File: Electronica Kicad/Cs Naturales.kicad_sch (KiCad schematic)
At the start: 13 parts, among them M1 Motor_DC

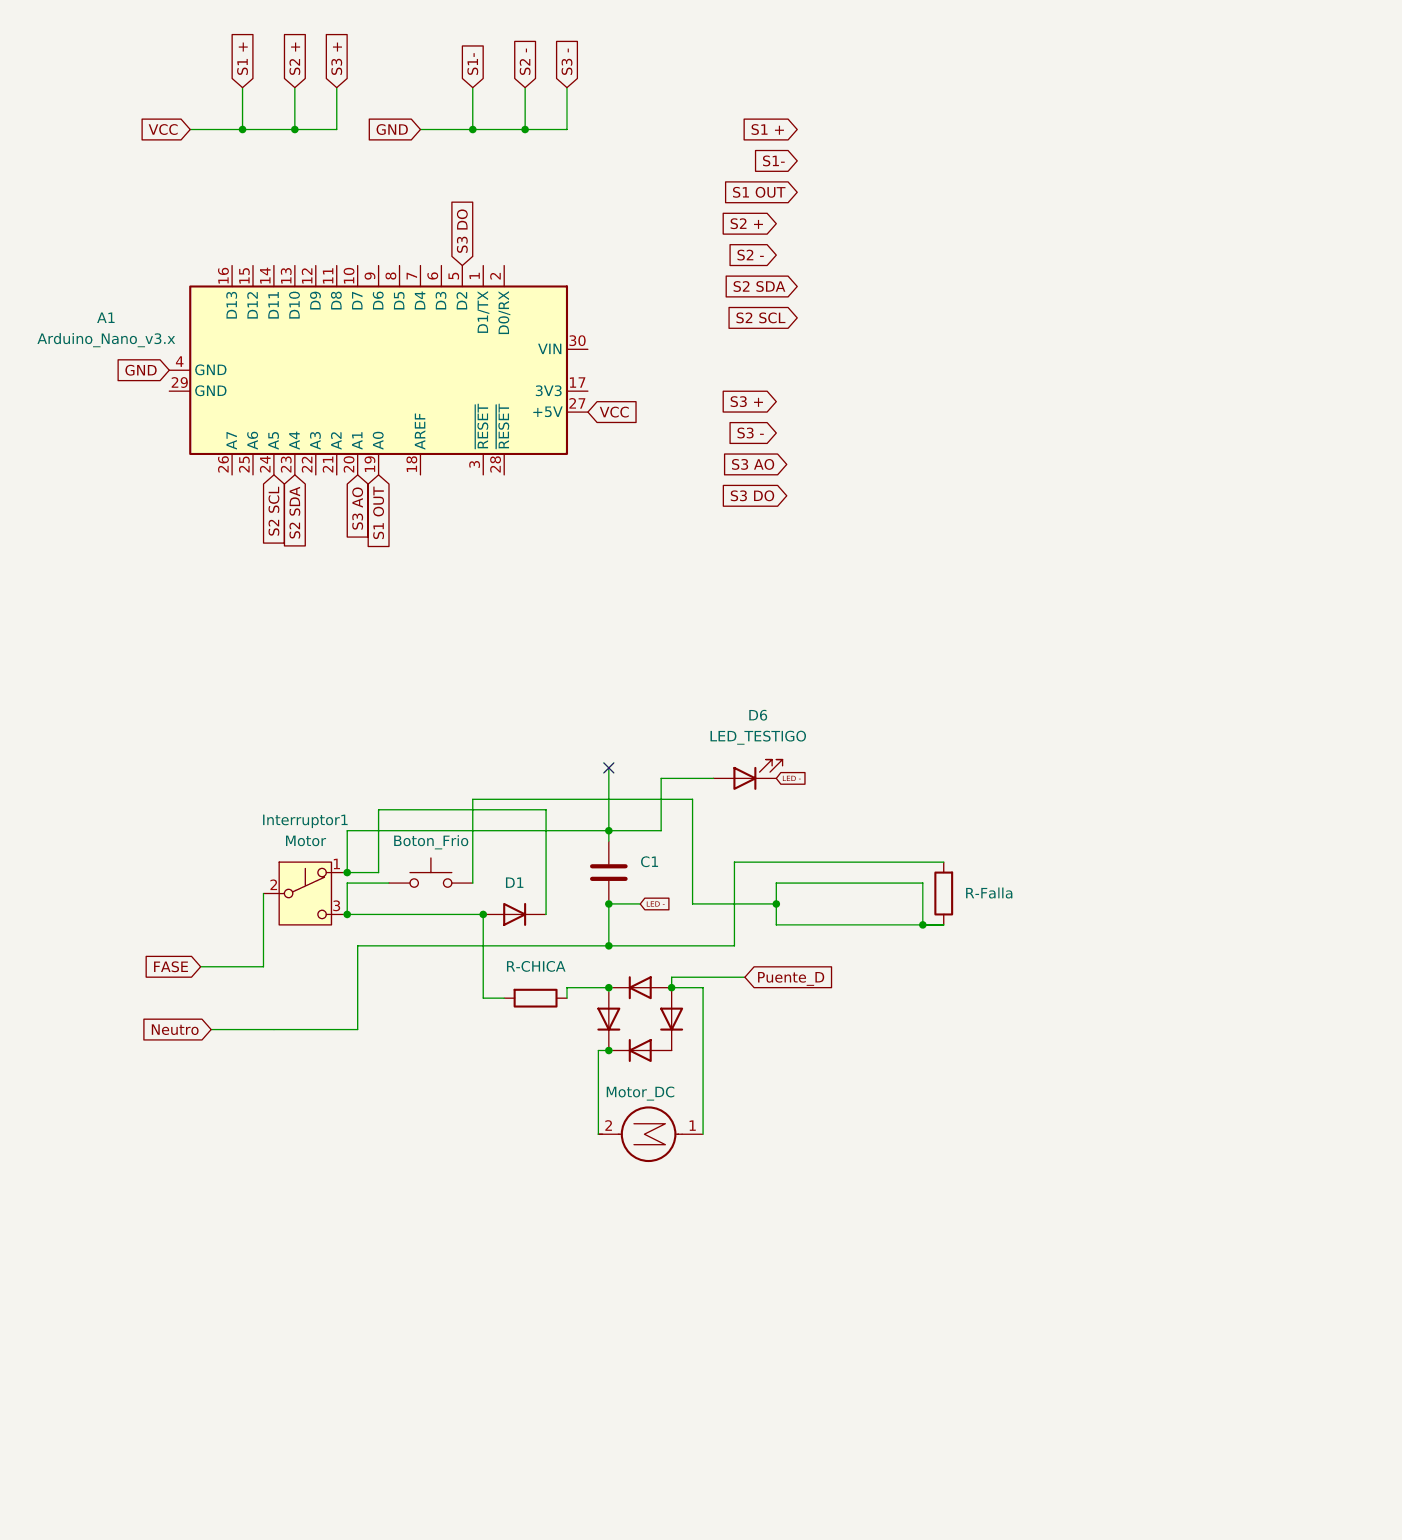
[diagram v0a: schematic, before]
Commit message: Modifico Archivo Esquematico y agrego ESP32 MOD
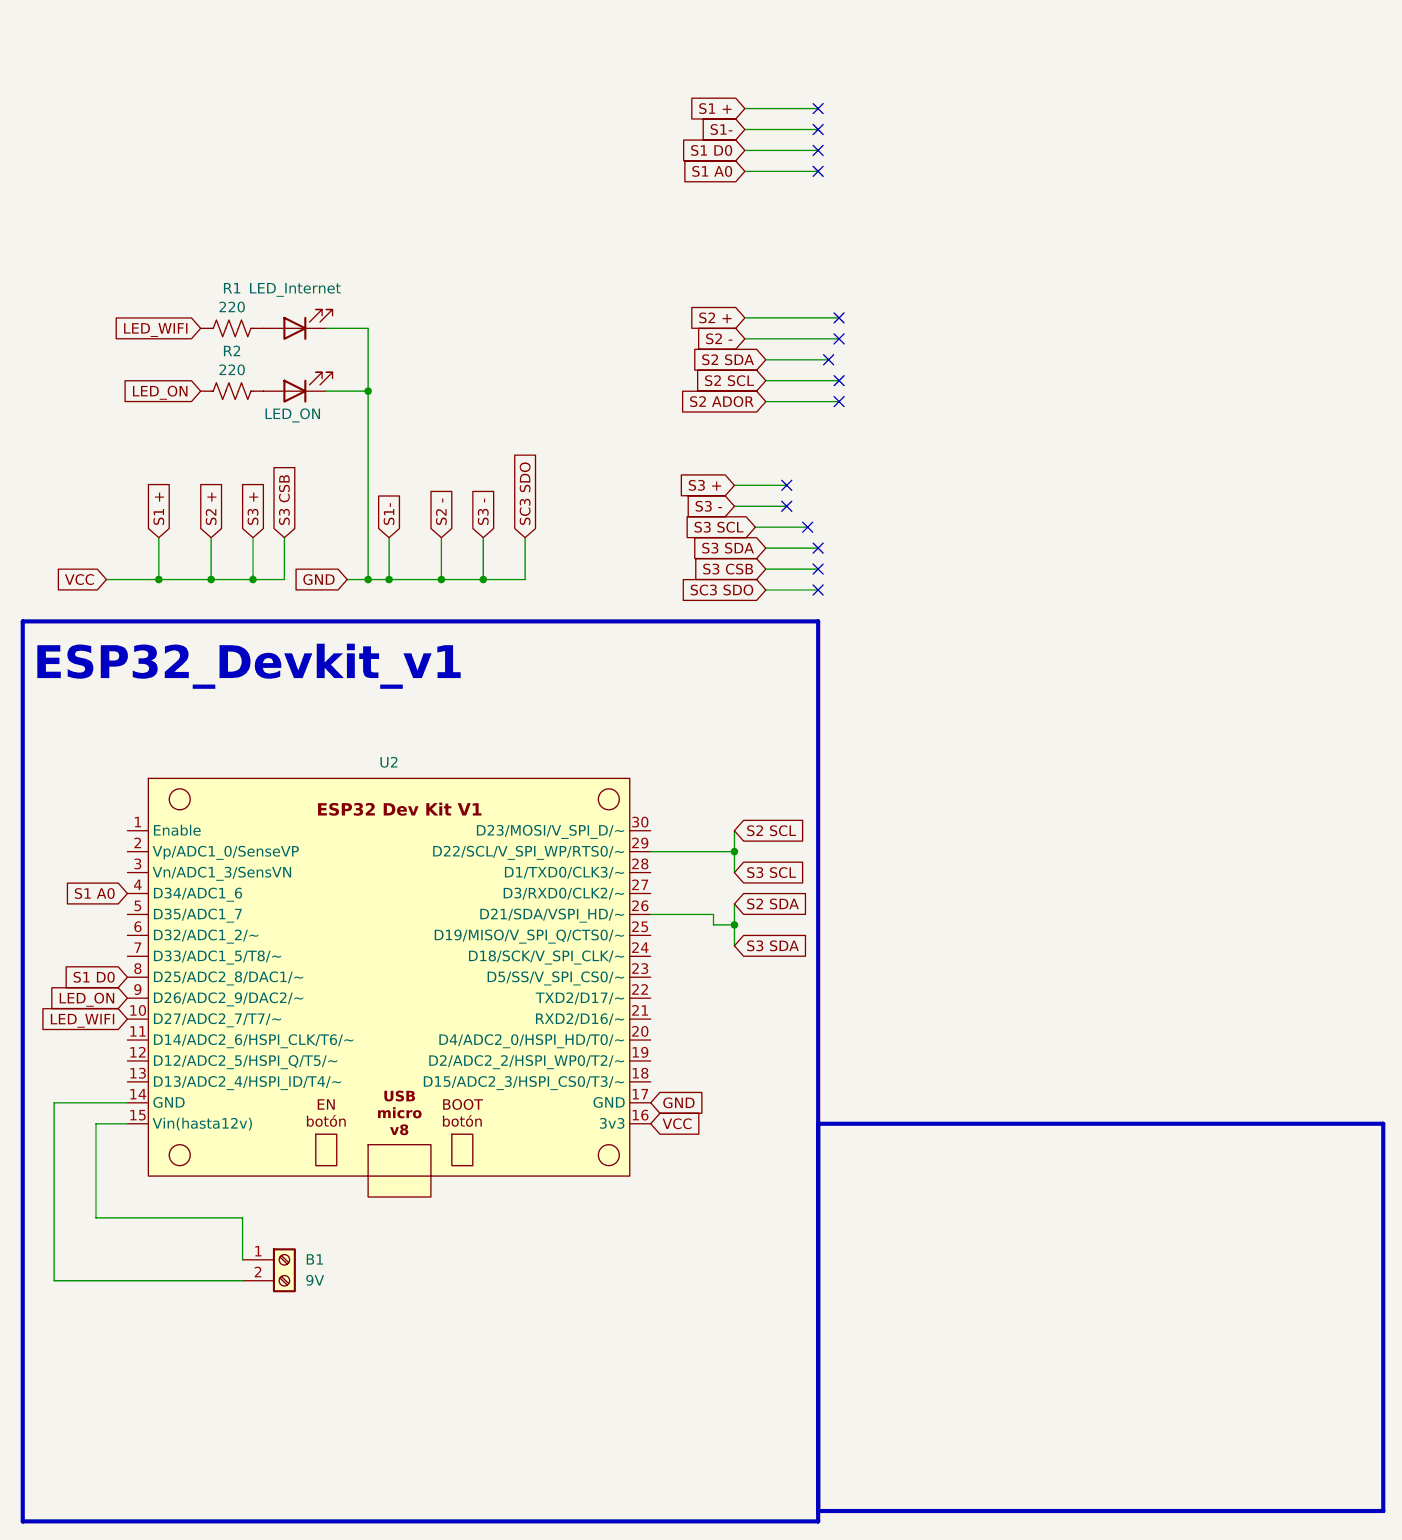
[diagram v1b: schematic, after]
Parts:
- removed A1: Arduino_Nano_v3.x, Module:Arduino_Nano, symbol MCU_Module:Arduino_Nano_v3.x
- removed Boton_Frio: SW_Push, symbol Switch:SW_Push
- removed C1: C, symbol Device:C
- removed D1, D3, D4, D5: D, symbol Device:D
- removed D2: D1, symbol Device:D
- removed D6: LED_TESTIGO, symbol Device:LED
- removed Interruptor1: Motor, symbol Switch:SW_Push_SPDT
- removed M1: Motor_DC, symbol Motor:Motor_DC
- removed R1: R-CHICA, symbol Device:R
- removed R3: R-Falla, symbol Device:R
- added B1: 9V, symbol Connector:Screw_Terminal_01x02
- added D1: LED_ON, symbol Device:LED
- added D2: LED_Internet, symbol Device:LED
- added R1, R2: 220, symbol Device:R_US
- added U2: ~, Librerias:ESP32-DevKit_V1, symbol EME:ESP32_DevKit_V1
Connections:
- net GND: now also D1.1 (K), D2.1 (K), U2.17 (GND)
- net S1 +: now also U2.16 (3v3)
- net S2 SCL: now also U2.29 (D22/SCL/V_SPI_WP/RTS0/~)
- net S2 SDA: now also U2.26 (D21/SDA/VSPI_HD/~)
- new net: D1.2 (A), R2.2
- new net: D2.2 (A), R1.2
- new net: B1.2 (Pin_2), U2.14 (GND)
- new net: B1.1 (Pin_1), U2.15 (Vin(hasta12v))
- new net LED_ON: R2.1, U2.9 (D26/ADC2_9/DAC2/~)
- new net LED_WIFI: R1.1, U2.10 (D27/ADC2_7/T7/~)
- new net S1 A0: U2.4 (D34/ADC1_6)
- new net S1 D0: U2.8 (D25/ADC2_8/DAC1/~)
- no-connect marks 1 -> 15
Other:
- note added: "ESP32_Devkit_v1"

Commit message: Modifico archivo Kicad
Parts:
- added D3: D, Diode_THT:D_DO-41_SOD81_P10.16mm_Horizontal, symbol Device:D
- B1: footprint (none) -> TerminalBlock_Phoenix:TerminalBlock_Phoenix_MKDS-1,5-2-5.08_1x02_P5.08mm_Horizontal
- D1: footprint (none) -> LED_THT:LED_D5.0mm
- D2: footprint (none) -> LED_THT:LED_D5.0mm_Clear
- M1: renamed from U2; footprint Librerias:ESP32-DevKit_V1 -> Librerias1:ESP32-DevKit_V1
- R1, R2: footprint (none) -> Resistor_THT:R_Axial_DIN0204_L3.6mm_D1.6mm_P5.08mm_Horizontal
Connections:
- net at M1.15 (Vin(hasta12v)): now also D3.1 (K); no longer B1.1 (Pin_1)
- new net: B1.1 (Pin_1), D3.2 (A)
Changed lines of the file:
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@@
+	(wire
+		(pts
+			(xy 35.56 161.29) (xy 39.37 161.29)
+		)
+		(stroke
+			(width 0)
+			(type default)
+			(color 255 0 0 1)
+		)
+	)
 	(wire
 		(pts
@@
 	(wire
 		(pts
+			(xy 21.59 161.29) (xy 27.94 161.29)
+		)
+		(stroke
+			(width 0)
+			(type default)
+			(color 255 0 0 1)
+		)
+	)
+	(wire
+		(pts
 			(xy 54.61 60.96) (xy 54.61 83.82)
 		)
@@
 			(width 0)
 			(type default)
-		)
-	)
-	(wire
-		(pts
-			(xy 21.59 161.29) (xy 39.37 161.29)
-		)
-		(stroke
-			(width 0)
-			(type default)
-			(color 255 0 0 1)
 		)
 	)
@@
 			)
 		)
-		(property "Footprint" ""
+		(property "Footprint" "LED_THT:LED_D5.0mm"
 			(at 45.72 60.96 0)
 			(effects
@@
 			)
 		)
-		(property "Footprint" ""
+		(property "Footprint" "Resistor_THT:R_Axial_DIN0204_L3.6mm_D1.6mm_P5.08mm_Horizontal"
 			(at 38.354 52.324 90)
 			(effects
@@
 		(dnp no)
 		(fields_autoplaced yes)
-		(property "Reference" "U2"
-			(at 57.15 106.045 0)
+		(property "Reference" "M1"
+			(at 57.15 105.41 0)
 			(effects
 				(font
@@
 					(size 1.27 1.27)
 				)
-			)
-		)
-		(property "Footprint" "Librerias:ESP32-DevKit_V1"
+				(hide yes)
+			)
+		)
+		(property "Footprint" "Librerias1:ESP32-DevKit_V1"
 			(at 58.42 105.41 0)
 			(effects
@@
 			(project "Cs Naturales"
 				(path "/11f292c7-2d24-408b-b314-b6582b54f0a5"
-					(reference "U2")
+					(reference "M1")
 					(unit 1)
 				)
@@
 			)
 		)
-		(property "Footprint" ""
+		(property "Footprint" "LED_THT:LED_D5.0mm_Clear"
 			(at 45.72 53.34 0)
 			(effects
@@
 			)
 		)
-		(property "Footprint" ""
+		(property "Footprint" "TerminalBlock_Phoenix:TerminalBlock_Phoenix_MKDS-1,5-2-5.08_1x02_P5.08mm_Horizontal"
 			(at 44.45 166.37 0)
 			(effects
@@
 				(path "/11f292c7-2d24-408b-b314-b6582b54f0a5"
 					(reference "B1")
+					(unit 1)
+				)
+			)
+		)
+	)
+	(symbol
+		(lib_id "Device:D")
+		(at 31.75 161.29 0)
+		(unit 1)
+		(exclude_from_sim no)
+		(in_bom yes)
+		(on_board yes)
+		(dnp no)
+		(fields_autoplaced yes)
+		(property "Reference" "D3"
+			(at 31.75 154.94 0)
+			(effects
+				(font
+					(size 1.27 1.27)
+				)
+				(hide yes)
+			)
+		)
+		(property "Value" "D"
+			(at 31.75 157.48 0)
+			(effects
+				(font
+					(size 1.27 1.27)
+				)
+				(hide yes)
+			)
+		)
+		(property "Footprint" "Diode_THT:D_DO-41_SOD81_P10.16mm_Horizontal"
+			(at 31.75 161.29 0)
+			(effects
+				(font
+					(size 1.27 1.27)
+				)
+				(hide yes)
+			)
+		)
+		(property "Datasheet" "~"
+			(at 31.75 161.29 0)
+			(effects
+				(font
+					(size 1.27 1.27)
+				)
+				(hide yes)
+			)
+		)
+		(property "Description" "Diode"
+			(at 31.75 161.29 0)
+			(effects
+				(font
+					(size 1.27 1.27)
+				)
+				(hide yes)
+			)
+		)
+		(property "Sim.Device" "D"
+			(at 31.75 161.29 0)
+			(effects
+				(font
+					(size 1.27 1.27)
+				)
+				(hide yes)
+			)
+		)
+		(property "Sim.Pins" "1=K 2=A"
+			(at 31.75 161.29 0)
+			(effects
+				(font
+					(size 1.27 1.27)
+				)
+				(hide yes)
+			)
+		)
+		(pin "2"
+		)
+		(pin "1"
+		)
+		(instances
+			(project ""
+				(path "/11f292c7-2d24-408b-b314-b6582b54f0a5"
+					(reference "D3")
 					(unit 1)
 				)
@@
 			)
 		)
-		(property "Footprint" ""
+		(property "Footprint" "Resistor_THT:R_Axial_DIN0204_L3.6mm_D1.6mm_P5.08mm_Horizontal"
 			(at 38.354 59.944 90)
 			(effects

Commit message: Diseño PCB listo
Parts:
- added S1: Conn_01x04_MountingPin, Connector_PinHeader_1.00mm:PinHeader_1x04_P1.00mm_Vertical, symbol Connector_Generic_MountingPin:Conn_01x04_MountingPin
- added S2: Conn_01x05_MountingPin, Connector_PinHeader_1.00mm:PinHeader_1x05_P1.00mm_Vertical, symbol Connector_Generic_MountingPin:Conn_01x05_MountingPin
- added S3: Conn_01x06_MountingPin, Connector_PinHeader_1.00mm:PinHeader_1x06_P1.00mm_Vertical, symbol Connector_Generic_MountingPin:Conn_01x06_MountingPin
- M1: footprint Librerias1:ESP32-DevKit_V1 -> ESP32_ Naturales:ESP32-DevKit_V1
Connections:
- net GND: now also S1.2 (Pin_2), S2.2 (Pin_2), S3.2 (Pin_2), S3.6 (Pin_6)
- net LED_ON: now also M1.10 (D27/ADC2_7/T7/~); no longer M1.9 (D26/ADC2_9/DAC2/~)
- net LED_WIFI: now also M1.9 (D26/ADC2_9/DAC2/~); no longer M1.10 (D27/ADC2_7/T7/~)
- net S1 +: now also S1.1 (Pin_1), S2.1 (Pin_1), S3.1 (Pin_1), S3.5 (Pin_5)
- net S1 A0: now also S1.4 (Pin_4)
- net S1 D0: now also S1.3 (Pin_3)
- net S2 ADOR: now also S2.5 (Pin_5)
- net S2 SCL: now also S2.4 (Pin_4), S3.3 (Pin_3)
- net S2 SDA: now also S2.3 (Pin_3), S3.4 (Pin_4)
- no-connect marks 15 -> 0
